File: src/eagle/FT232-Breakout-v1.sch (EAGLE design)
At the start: 15 parts, among them T1 BC547, U1 FT232RL-BASICSSOP

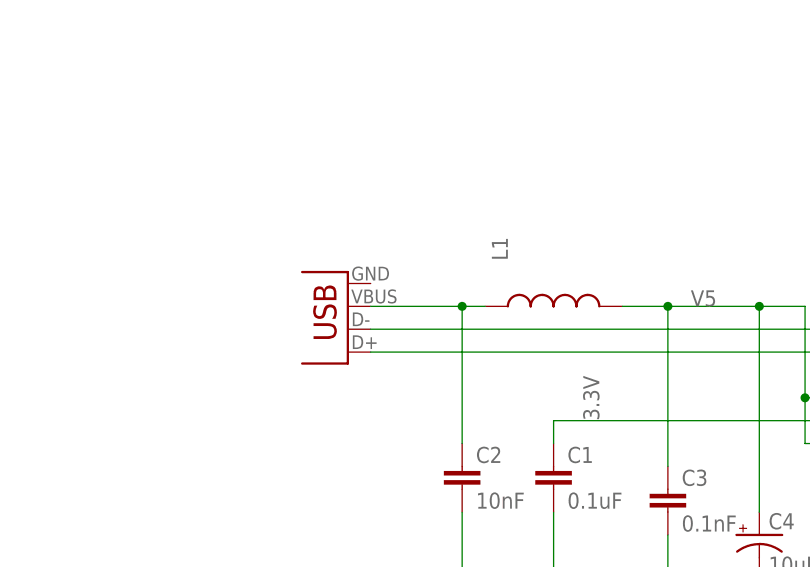
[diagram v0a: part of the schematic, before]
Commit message: modified daughter board for production
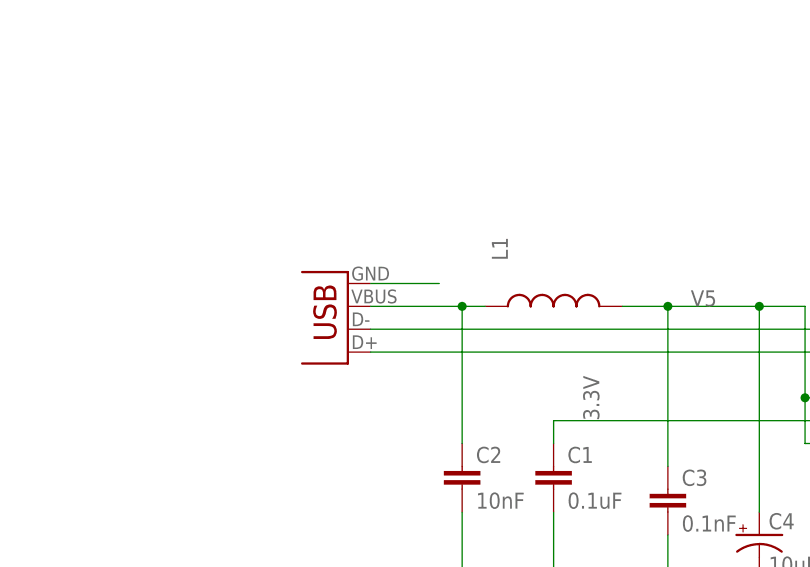
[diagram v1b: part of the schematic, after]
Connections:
- net GND: now also JP1.GND
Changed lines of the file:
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@@
 <grid distance="0.1" unitdist="inch" unit="inch" style="lines" multiple="1" display="no" altdistance="0.01" altunitdist="inch" altunit="inch"/>
 <layers>
-<layer number="1" name="Top" color="4" fill="1" visible="yes" active="no"/>
-<layer number="16" name="Bottom" color="1" fill="1" visible="yes" active="no"/>
-<layer number="17" name="Pads" color="2" fill="1" visible="yes" active="no"/>
-<layer number="18" name="Vias" color="2" fill="1" visible="yes" active="no"/>
-<layer number="19" name="Unrouted" color="6" fill="1" visible="yes" active="no"/>
-<layer number="20" name="Dimension" color="15" fill="1" visible="yes" active="no"/>
-<layer number="21" name="tPlace" color="7" fill="1" visible="yes" active="no"/>
-<layer number="22" name="bPlace" color="7" fill="1" visible="yes" active="no"/>
-<layer number="23" name="tOrigins" color="15" fill="1" visible="yes" active="no"/>
-<layer number="24" name="bOrigins" color="15" fill="1" visible="yes" active="no"/>
-<layer number="25" name="tNames" color="7" fill="1" visible="yes" active="no"/>
-<layer number="26" name="bNames" color="7" fill="1" visible="yes" active="no"/>
-<layer number="27" name="tValues" color="7" fill="1" visible="yes" active="no"/>
-<layer number="28" name="bValues" color="7" fill="1" visible="yes" active="no"/>
+<layer number="1" name="Top" color="4" fill="1" visible="no" active="no"/>
+<layer number="16" name="Bottom" color="1" fill="1" visible="no" active="no"/>
+<layer number="17" name="Pads" color="2" fill="1" visible="no" active="no"/>
+<layer number="18" name="Vias" color="2" fill="1" visible="no" active="no"/>
+<layer number="19" name="Unrouted" color="6" fill="1" visible="no" active="no"/>
+<layer number="20" name="Dimension" color="15" fill="1" visible="no" active="no"/>
+<layer number="21" name="tPlace" color="7" fill="1" visible="no" active="no"/>
+<layer number="22" name="bPlace" color="7" fill="1" visible="no" active="no"/>
+<layer number="23" name="tOrigins" color="15" fill="1" visible="no" active="no"/>
+<layer number="24" name="bOrigins" color="15" fill="1" visible="no" active="no"/>
+<layer number="25" name="tNames" color="7" fill="1" visible="no" active="no"/>
+<layer number="26" name="bNames" color="7" fill="1" visible="no" active="no"/>
+<layer number="27" name="tValues" color="7" fill="1" visible="no" active="no"/>
+<layer number="28" name="bValues" color="7" fill="1" visible="no" active="no"/>
 <layer number="29" name="tStop" color="7" fill="3" visible="no" active="no"/>
 <layer number="30" name="bStop" color="7" fill="6" visible="no" active="no"/>
@@
 <layer number="35" name="tGlue" color="7" fill="4" visible="no" active="no"/>
 <layer number="36" name="bGlue" color="7" fill="5" visible="no" active="no"/>
-<layer number="37" name="tTest" color="7" fill="1" visible="yes" active="no"/>
-<layer number="38" name="bTest" color="7" fill="1" visible="yes" active="no"/>
+<layer number="37" name="tTest" color="7" fill="1" visible="no" active="no"/>
+<layer number="38" name="bTest" color="7" fill="1" visible="no" active="no"/>
 <layer number="39" name="tKeepout" color="4" fill="11" visible="no" active="no"/>
 <layer number="40" name="bKeepout" color="1" fill="11" visible="no" active="no"/>
@@
 <layer number="44" name="Drills" color="7" fill="1" visible="no" active="no"/>
 <layer number="45" name="Holes" color="7" fill="1" visible="no" active="no"/>
-<layer number="46" name="Milling" color="3" fill="1" visible="yes" active="no"/>
-<layer number="47" name="Measures" color="7" fill="1" visible="yes" active="no"/>
-<layer number="48" name="Document" color="7" fill="1" visible="yes" active="no"/>
-<layer number="49" name="Reference" color="7" fill="1" visible="yes" active="no"/>
-<layer number="50" name="dxf" color="7" fill="1" visible="yes" active="no"/>
-<layer number="51" name="tDocu" color="7" fill="1" visible="yes" active="no"/>
-<layer number="52" name="bDocu" color="7" fill="1" visible="yes" active="no"/>
-<layer number="53" name="tGND_GNDA" color="7" fill="9" visible="yes" active="no"/>
-<layer number="54" name="bGND_GNDA" color="1" fill="9" visible="yes" active="no"/>
-<layer number="56" name="wert" color="7" fill="1" visible="yes" active="no"/>
+<layer number="46" name="Milling" color="3" fill="1" visible="no" active="no"/>
+<layer number="47" name="Measures" color="7" fill="1" visible="no" active="no"/>
+<layer number="48" name="Document" color="7" fill="1" visible="no" active="no"/>
+<layer number="49" name="Reference" color="7" fill="1" visible="no" active="no"/>
+<layer number="50" name="dxf" color="7" fill="1" visible="no" active="no"/>
+<layer number="51" name="tDocu" color="7" fill="1" visible="no" active="no"/>
+<layer number="52" name="bDocu" color="7" fill="1" visible="no" active="no"/>
+<layer number="53" name="tGND_GNDA" color="7" fill="9" visible="no" active="no"/>
+<layer number="54" name="bGND_GNDA" color="1" fill="9" visible="no" active="no"/>
+<layer number="56" name="wert" color="7" fill="1" visible="no" active="no"/>
 <layer number="91" name="Nets" color="2" fill="1" visible="yes" active="yes"/>
 <layer number="92" name="Busses" color="1" fill="1" visible="yes" active="yes"/>
@@
 <label x="104.14" y="91.44" size="1.778" layer="95"/>
 </segment>
-</net>
+<segment>
+<pinref part="JP1" gate="G$1" pin="GND"/>
+<wire x1="27.94" y1="157.48" x2="35.56" y2="157.48" width="0.1524" layer="91"/>
+</segment>
+</net>
